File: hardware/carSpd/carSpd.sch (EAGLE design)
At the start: 0 parts

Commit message: Added power regulator schematics
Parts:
- added C1: 10uf, rcl:C-EUC0603K
- added C2: 22uf, rcl:C-EUC0603K
- added C3: 3.9nf, rcl:C-EUC0603K
- added C4, C7: .1uf, rcl:C-EUC0603K
- added C5: 10nf, rcl:C-EUC0603K
- added C6: .33uf, rcl:C-EUC0603K
- added IC1: DS3231/SO, adafruit:DS3231/SO
- added IC2: CP2102, silabs:CP2102
- added IC3: 7805DT, adafruit:7805DT
- added L1: CD54, inductor-sumida:CD54
- added L2: 10uh, rcl:L-USL3225M
- added R1: 10k, rcl:R-US_R0603
- added R2: 100k, rcl:R-US_R0603
- added R3: 6.8k, rcl:R-US_R0603
- added R4: 44.2k, rcl:R-US_R0603
- added S1, S2, S3, S4: SWITCH-MOMENTARY-2SMD-4, SparkFun-Electromechanical:SWITCH-MOMENTARY-2SMD-4
- added U$1: CH340G, ch340g:CH340G
- added U1: ATMEGA328P-AU, Atmel_By_element14_Batch_1-00:ATMEGA328P-AU
- added U2: MP2307, hybridair:MP2307
- added U3: ERC1602-4, hybridair:ERC1602-4
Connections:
- new net +12V: C1.1, C6.1, IC3.VI, R2.2, U2.IN
- new net +5V: C2.1, C7.1, IC3.VO, L1.1, L2.1, R4.1
- new net GND: C1.2, C2.2, C4.2, C6.2, C7.2, IC3.GND, R1.1, R3.1, U2.GND
- new net N$1: C5.2, U2.BS
- new net N$2: C5.1, L1.2, L2.2, U2.SW
- new net N$3: R1.2, R4.2, U2.FB
- new net N$5: C3.2, R3.2
- new net N$6: C3.1, U2.COMP
- new net N$7: C4.1, U2.SS
- new net N$9: R2.1, U2.EN
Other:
- note added: "12V comes from the car's accessory power rail, which is regulated down to 5V. The carSpd device itself shouldn't use more than 100ma."
- note added: "For option 1, use either the 10uh CD54 inductor or 10uh 3225 inductor. Either one should support at least 500ma of current saturation."
- note added: "ONLY USE ONE OPTION, DO NOT POPULATE BOTH AT ONCE"
- note added: "OPTION 1"
- note added: "OPTION 2"
- note added: "Option 1 is an untested DC-DC buck regulator, and Option 2 is a tested, backup linear regulator circuit. Option 1 is preferred due to its efficiency, but is untested so it may not work in production. Option 2 is simpler, less efficient, but should work as expected."
- note added: "POWER REGULATION"

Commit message: Added USB to serial schematics
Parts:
- removed IC3: 7805DT, adafruit:7805DT
- added C10, C11, C15, C9: 0.1uf, rcl:C-EUC0603K
- added C12: 10nf, rcl:C-EUC0603K
- added C13, C14: 18pf, rcl:C-EUC0603K
- added C8: 1uf, rcl:C-EUC0603K
- added JP1: USBSMD, SparkFun-Connectors:USBSMD
- added R6: 4.7k, rcl:R-US_R0603
- added R7: 10k, rcl:R-US_R0603
- added U4: ERC1602-4, hybridair:ERC1602-4
- added Y1: 12mhz, SparkFun-FreqCtrl:CRYSTALFIXED
- added Y2: (no value), SparkFun-FreqCtrl:CRYSTALSMD
- U3: value ERC1602-4 -> 7805DT; device hybridair:ERC1602-4 -> adafruit:7805DT
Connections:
- new net D+: IC2.D+, U$1.D+
- new net D-: IC2.D-, U$1.D-
- new net N$10: C11.1, IC2.DTR
- new net N$12: C10.1, IC2.VDD
- new net N$16: C15.1, U$1.DTR
- new net N$17: C12.1, U$1.V3
- new net N$18: C14.2, U$1.XO, Y1.2, Y2.2
- new net N$19: C13.2, U$1.XI, Y1.1, Y2.1
- new net N$4: IC2.!RST, R6.1
- new net N$8: IC2.!SUSPEND, R7.2
- new net RST: C11.2, C15.2
- new net RX: IC2.TXD, U$1.TX
- new net TX: IC2.RXD, U$1.RX
- net +12V: now also U3.VI; no longer IC3.VI
- net +5V: now also C8.1, C9.1, IC2.REGIN, IC2.VBUS, R6.2, U$1.VCC, U3.VO; no longer IC3.VO
- net GND: now also C10.2, C12.2, C13.1, C14.1, C8.2, C9.2, IC2.GND, IC2.GND@EXP, IC2.GND@M, R7.1, U$1.GND, U3.GND; no longer IC3.GND
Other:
- note added: "For option 1, use either an SMD axial crystal, or an SMD HC49 crystal. Change load capacitors as necessary."
- note added: "Option 1 is an untested CH340G serial circuit, and Option 2 is a tested, backup CP2102 serial circuit. Option 1 is preferred due to its price, but is untested so it may not work in production. Option 2 is more expensive, but will work just fine."
- note added: "The USB to serial circuit is used to allow the atmega328 to be programmed over USB, using the optiboot serial bootloader."
- note added: "USB to Serial"

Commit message: Added peripheral schematics
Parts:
- removed U4: ERC1602-4, hybridair:ERC1602-4
- added B1: BATTERY1220, Battery&Holder:BATTERY1220
- added C16, C20: 0.1uf, rcl:C-EUC0603K
- added C17, C19: 1uf, rcl:C-EUC0603K
- added C18: 10uf, rcl:C-EUC0603K
- added DISPLAY: ERC1602-4, hybridair:ERC1602-4
- added DISP_LED: (no value), SparkFun-Connectors:M021X02_NO_SILK
- added LED1, LED2, LED3, LED4: (no value), led:LEDCHIPLED_0805
- added Q1: 2n3904, SparkFun-DiscreteSemi:TRANSISTOR_NPNSOT23-3
- added R10, R9: 4.7k, rcl:R-US_R0603
- added R5: 10k, rcl:R-US_R0603
- added R8: 220, rcl:R-US_R0603
- added U$2: DS1820, Ava:DS1820
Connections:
- new net LED_PWM: R5.2
- new net N$11: Q1.B, R5.1
- new net N$13: DISP_LED.2, R8.1
- new net N$14: C17.2, DISPLAY.VOUT
- new net N$15: Q1.C, R8.2, R9.2
- new net N$20: C19.1, DISPLAY.CAP1P
- new net N$21: C19.2, DISPLAY.CAP1N
- new net N$23: LED1.A, LED2.A, LED3.A, LED4.A, R9.1
- new net N$27: B1.+, IC1.VBAT
- new net SCL: DISPLAY.SCL, IC1.SCL
- new net SDA: DISPLAY.SDA, IC1.SDA
- new net TEMP: R10.1, U$2.DQ
- net +5V: now also C16.1, C17.1, C18.1, C20.1, DISPLAY.PSB, DISPLAY.RS, DISPLAY.VDD, DISPLAY.XRESET, IC1.VCC, R10.2, U$2.VCC
- net GND: now also B1.-, C16.2, C18.2, C20.2, DISPLAY.CSB, DISPLAY.PSI2B, DISPLAY.VSS, DISP_LED.1, IC1.GND, IC1.NC, IC1.NC1, IC1.NC2, IC1.NC3, IC1.NC4, IC1.NC5, IC1.NC6, IC1.NC7, LED1.C, LED2.C, LED3.C, LED4.C, Q1.E, U$2.GND
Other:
- note added: "DISPLAY"
- note added: "Peripherals"
- note added: "RTC"
- note added: "TEMP"
- note added: "The DS3231 RTC is untested, but should wor according to the datasheet."

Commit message: Finished schematic, unverified
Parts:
- removed U1: ATMEGA328P-AU, Atmel_By_element14_Batch_1-00:ATMEGA328P-AU
- added C22, C23: 18pf, rcl:C-EUC0603K
- added C24, C25: 0.1uf, rcl:C-EUC0603K
- added D1, D2, D3: 5.1V, SparkFun-DiscreteSemi:DIODE-ZENER5.6V
- added JP2: AVR_ICSP, SparkFun-Connectors:AVR_SPI_PRG_6TESTPOINTS
- added JP3: USBSMD, SparkFun-Connectors:USBSMD
- added LED5: STATUS, led:LEDCHIPLED_0805
- added LED6: POWER, led:LEDCHIPLED_0805
- added R11: 10k, rcl:R-US_R0603
- added R12, R13: 4.7k, rcl:R-US_R0603
- added R14: 220, rcl:R-US_R0603
- added R15, R16, R17: 50k, rcl:R-US_R0603
- added R18: 1k, rcl:R-US_R0603
- added S5: RESET, SparkFun-Electromechanical:SWITCH-MOMENTARY-2SMD-1101NE
- added U$3, U$4, U$5: 5.1V, hybridair:ZMM5V1
- added U4: ATMEGA328P_TQFP, SparkFun-DigitalIC:ATMEGA328P_TQFP
- added Y3: 16mhz, SparkFun-FreqCtrl:CRYSTALSMD
- JP1: value USBSMD -> CAR_INPUT; device SparkFun-Connectors:USBSMD -> SparkFun-Connectors:M05PTH
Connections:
- new net INJ: JP1.3, R15.1
- new net LIGHTING: JP1.4, R17.1
- new net N$22: JP2.1, U4.PB4(MISO)
- new net N$24: C22.1, U4.PB6(XTAL1/TOSC1), Y3.2
- new net N$26: JP2.3, LED5.A, U4.PB5(SCK)
- new net N$28: S1.1, U4.PD6(AIN0)
- new net N$29: LED6.A, R18.1
- new net N$30: D2.C, R15.2, U$4.C, U4.PD2(INT0), U4.PD3(INT1)
- new net N$31: D1.C, R17.2, U$3.C, U4.PC0(ADC0)
- new net N$32: LED5.C, R14.1
- new net N$33: S3.1, U4.PB0(ICP)
- new net N$34: S2.1, U4.PD7(AIN1)
- new net N$35: S4.1, U4.PB1(OC1A)
- new net N$36: D3.C, R16.2, U$5.C, U4.PD5(T1)
- new net N$37: C23.1, U4.PB7(XTAL2/TOSC2), Y3.1
- new net VSS: JP1.2, R16.1
- net +12V: now also JP1.1
- net +5V: now also C24.1, C25.1, JP2.2, JP3.VBUS, R11.1, R12.1, R13.1, R18.2, U4.AVCC, U4.VCC@4, U4.VCC@6
- net D+: now also JP3.D+
- net D-: now also JP3.D-
- net GND: now also C22.2, C23.2, C24.2, C25.2, D1.A, D2.A, D3.A, JP1.5, JP2.6, JP3.GND, LED6.C, R14.2, S1.2, S2.2, S3.2, S4.2, S5.1, U$3.A, U$4.A, U$5.A, U4.AGND, U4.GND@3, U4.GND@5
- net LED_PWM: now also JP2.4, U4.PB3(MOSI/OC2)
- net RST: now also JP2.5, R11.2, S5.2, U4.PC6(/RESET)
- net RX: now also U4.PD0(RXD)
- net SCL: now also R13.2, U4.PC5(ADC5/SCL)
- net SDA: now also R12.2, U4.PC4(ADC4/SDA)
- net TX: now also U4.PD1(TXD)
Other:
- note added: "The DS3231 RTC is untested, but should work according to the datasheet."
- note added: "Two crystal footprints are provided for part compatibility, use only one."
- note added: "Two diode footprints are provided for part compatibility, use only one."
- note removed: "For option 1, use either an SMD axial crystal, or an SMD HC49 crystal. Change load capacitors as necessary."
- note removed: "The DS3231 RTC is untested, but should wor according to the datasheet."

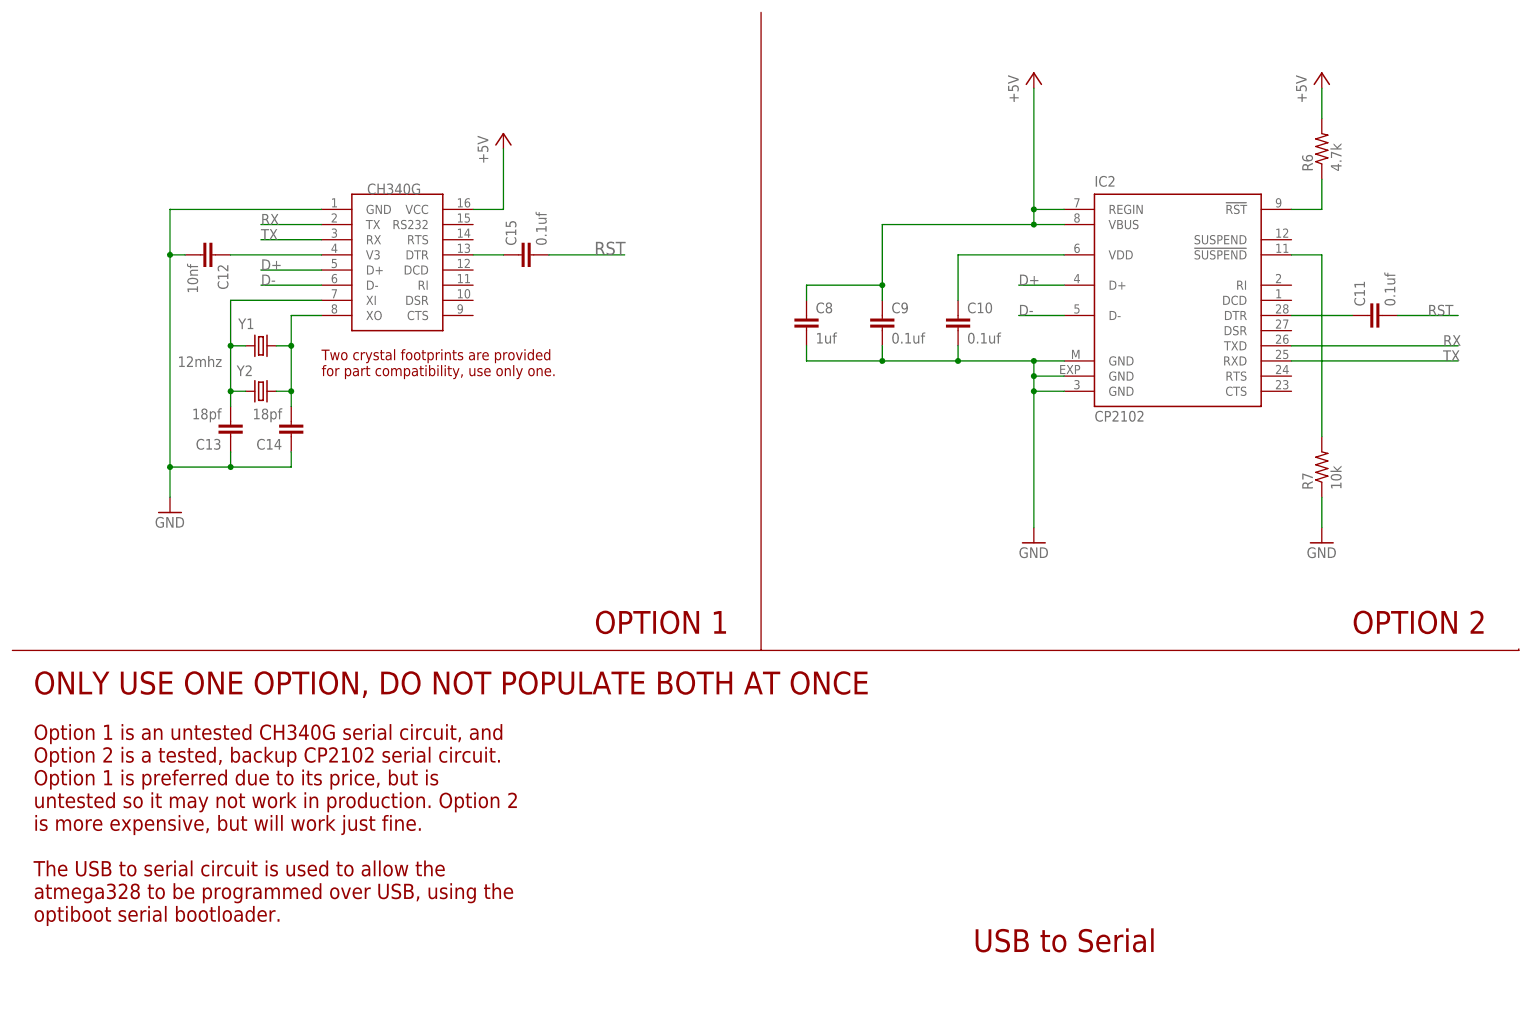
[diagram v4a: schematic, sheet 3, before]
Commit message: Removed the CH340G, supporting parts made it cost as much as a CP2102
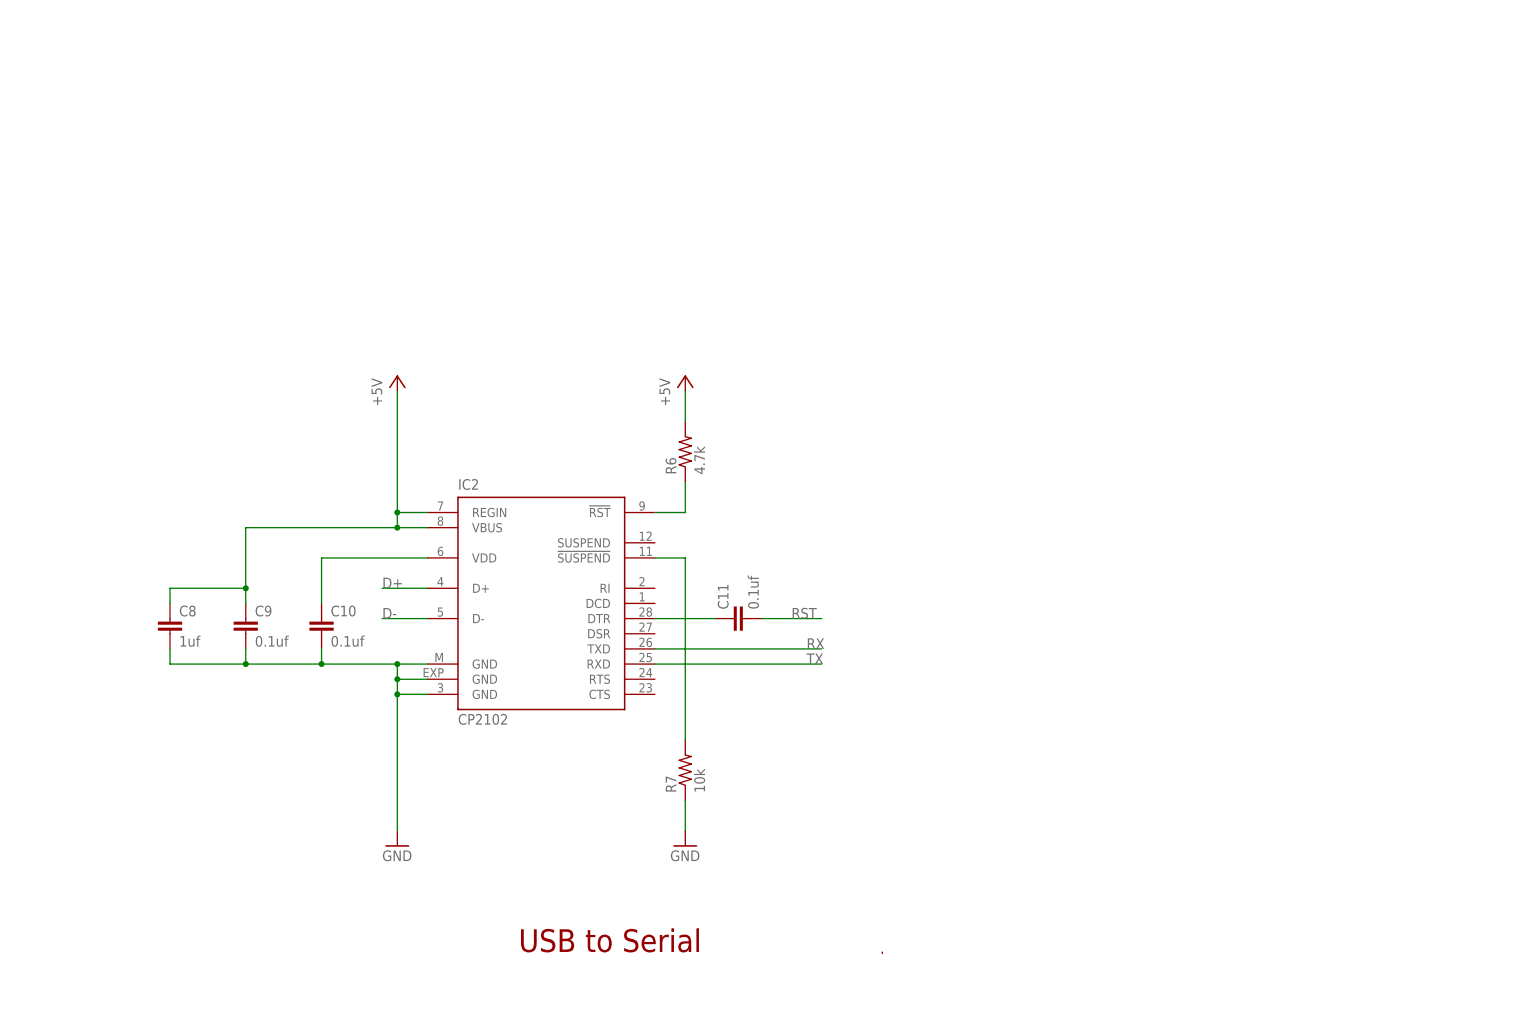
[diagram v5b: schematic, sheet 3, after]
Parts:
- removed C12: 10nf, rcl:C-EUC0603K
- removed C13, C14: 18pf, rcl:C-EUC0603K
- removed C15: 0.1uf, rcl:C-EUC0603K
- removed JP1: CAR_INPUT, SparkFun-Connectors:M05PTH
- removed U$1: CH340G, ch340g:CH340G
- removed Y1: 12mhz, SparkFun-FreqCtrl:CRYSTALFIXED
- removed Y2: (no value), SparkFun-FreqCtrl:CRYSTALSMD
- added STANDOFF1, STANDOFF2, STANDOFF3, STANDOFF4: STAND-OFF, SparkFun-Electromechanical:STAND-OFF
- added SV1: CAR_INPUT, con-lsta:FE05W
- S1, S2, S3, S4: value SWITCH-MOMENTARY-2SMD-4 -> SWITCH-MOMENTARY-2SMD-1101NE; device SparkFun-Electromechanical:SWITCH-MOMENTARY-2SMD-4 -> SparkFun-Electromechanical:SWITCH-MOMENTARY-2SMD-1101NE
- Y3: device SparkFun-FreqCtrl:CRYSTALSMD -> SparkFun-FreqCtrl:CRYSTAL5X3
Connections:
- removed net N$16: C15.1, U$1.DTR
- removed net N$17: C12.1, U$1.V3
- removed net N$18: C14.2, U$1.XO, Y1.2, Y2.2
- removed net N$19: C13.2, U$1.XI, Y1.1, Y2.1
- net +12V: now also SV1.1; no longer JP1.1
- net +5V: no longer U$1.VCC
- net D+: no longer U$1.D+
- net D-: no longer U$1.D-
- net GND: now also SV1.5; no longer C12.2, C13.1, C14.1, JP1.5, U$1.GND
- net INJ: now also SV1.3; no longer JP1.3
- net LIGHTING: now also SV1.4; no longer JP1.4
- net RST: no longer C15.2
- net RX: no longer U$1.TX
- net TX: no longer U$1.RX
- net VSS: now also SV1.2; no longer JP1.2
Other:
- note added: "Two inductor footprints are provided for part compatibility, use only one."
- note removed: "For option 1, use either the 10uh CD54 inductor or 10uh 3225 inductor. Either one should support at least 500ma of current saturation."
- note removed: "Option 1 is an untested CH340G serial circuit, and Option 2 is a tested, backup CP2102 serial circuit. Option 1 is preferred due to its price, but is untested so it may not work in production. Option 2 is more expensive, but will work just fine."
- note removed: "The USB to serial circuit is used to allow the atmega328 to be programmed over USB, using the optiboot serial bootloader."
- note removed: "Two crystal footprints are provided for part compatibility, use only one."
- moved on the sheet: C10, C11, C8, C9, IC2, R6, R7

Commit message: Schematic cleanup
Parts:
- removed DISP_LED: (no value), SparkFun-Connectors:M021X02_NO_SILK
- removed STANDOFF1, STANDOFF2, STANDOFF3, STANDOFF4: STAND-OFF, SparkFun-Electromechanical:STAND-OFF
- removed U$3, U$4, U$5: 5.1V, hybridair:ZMM5V1
- removed Y3: 16mhz, SparkFun-FreqCtrl:CRYSTAL5X3
- added D4, D5, D6: 5.1V, hybridair:ZMM5V1
- added Y1: 16MHZ, SparkFun-FreqCtrl:RESONATOR16MHZ
- added Y2: 16mhz, SparkFun-FreqCtrl:CRYSTAL5X3
- B1: value BATTERY1220 -> CR1220
- C17, C19, C5, C8: device rcl:C-EUC0603K -> rcl:C-EUC0805K
- C4, C7: value .1uf -> 0.1uf
- DISPLAY: value ERC1602-4 -> ERC1602-4SMD-LED; device hybridair:ERC1602-4 -> hybridair:ERC1602-4SMD-LED
- R10, R12, R13, R2, R6, R9: device rcl:R-US_R0603 -> rcl:R-US_R0805
- R14: value 220 -> 270
- R15, R16, R17: value 50k -> 47k; device rcl:R-US_R0603 -> rcl:R-US_R0805
- R18: value 1k -> 2.7k
- R8: value 220 -> 150
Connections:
- removed net N$13: DISP_LED.2, R8.1
- new net N$16: DISPLAY.LED+, R8.1
- net GND: now also C23.1, D4.A, D5.A, D6.A, DISPLAY.LED-, Y1.2; no longer C23.2, DISP_LED.1, U$3.A, U$4.A, U$5.A
- net N$24: now also Y1.1, Y2.2; no longer Y3.2
- net N$30: now also D5.C; no longer U$4.C
- net N$31: now also D4.C; no longer U$3.C
- net N$36: now also D6.C; no longer U$5.C
- net N$37: now also C23.2, Y1.3, Y2.1; no longer C23.1, Y3.1
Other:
- note added: "Two crystal/ resonator footprints are provided for part compatibility, use only one."
- moved on the sheet: C17, C19, C22, C23, C24, C25, D1, D2, D3, JP2, LED5, R11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

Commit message: Modified and added parts list
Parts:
- C6: value .33uf -> 100uf; device rcl:C-EUC0603K -> ELL-i-Passives:CPOLD
- C7: value 0.1uf -> 10uf
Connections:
- net +12V: now also C6.+; no longer C6.1
- net GND: now also C6.-; no longer C6.2
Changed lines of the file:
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@@
 <layer number="56" name="wert" color="7" fill="1" visible="yes" active="no"/>
 <layer number="57" name="tCAD" color="7" fill="1" visible="yes" active="no"/>
+<layer number="58" name="bCopper" color="7" fill="1" visible="no" active="no"/>
 <layer number="59" name="tCarbon" color="7" fill="1" visible="yes" active="no"/>
 <layer number="60" name="bCarbon" color="7" fill="1" visible="yes" active="no"/>
@@
 <layer number="250" name="Descript" color="7" fill="1" visible="no" active="no"/>
 <layer number="251" name="SMDround" color="7" fill="1" visible="no" active="no"/>
+<layer number="253" name="Extra" color="7" fill="1" visible="yes" active="yes"/>
 <layer number="254" name="cooling" color="7" fill="1" visible="no" active="yes"/>
 <layer number="255" name="HELP" color="7" fill="1" visible="yes" active="yes"/>
@@
 <part name="P+3" library="supply1" deviceset="+12V" device=""/>
 <part name="U3" library="adafruit" deviceset="78*" device="DT" technology="05"/>
-<part name="C6" library="rcl" deviceset="C-EU" device="C0603K" value=".33uf"/>
-<part name="C7" library="rcl" deviceset="C-EU" device="C0603K" value="0.1uf"/>
+<part name="C7" library="rcl" deviceset="C-EU" device="C0603K" value="10uf"/>
 <part name="P+4" library="supply1" deviceset="+12V" device=""/>
 <part name="P+5" library="supply1" deviceset="+5V" device=""/>
@@
 <part name="FRAME5" library="frames" deviceset="A5L-LOC" device=""/>
 <part name="Y1" library="SparkFun-FreqCtrl" deviceset="RESONATOR" device="16MHZ" value="16MHZ"/>
+<part name="C6" library="ELL-i-Passives" deviceset="CPOL" device="D" value="100uf"/>
 </parts>
 <sheets>
@@
 <instances>
 <instance part="U3" gate="A1" x="208.28" y="129.54"/>
-<instance part="C6" gate="G$1" x="190.5" y="121.92"/>
 <instance part="C7" gate="G$1" x="226.06" y="121.92"/>
 <instance part="P+4" gate="1" x="190.5" y="142.24"/>
@@
 <instance part="P+3" gate="1" x="96.52" y="167.64"/>
 <instance part="FRAME4" gate="G$1" x="0" y="0"/>
+<instance part="C6" gate="G$1" x="190.5" y="121.92"/>
 </instances>
 <busses>
@@
 <net name="+12V" class="0">
 <segment>
-<pinref part="C6" gate="G$1" pin="1"/>
 <pinref part="P+4" gate="1" pin="+12V"/>
 <wire x1="190.5" y1="124.46" x2="190.5" y2="129.54" width="0.1524" layer="91"/>
@@
 <wire x1="190.5" y1="129.54" x2="198.12" y2="129.54" width="0.1524" layer="91"/>
 <junction x="190.5" y="129.54"/>
+<pinref part="C6" gate="G$1" pin="+"/>
 </segment>
 <segment>
@@
 <net name="GND" class="0">
 <segment>
-<pinref part="C6" gate="G$1" pin="2"/>
 <wire x1="190.5" y1="116.84" x2="190.5" y2="114.3" width="0.1524" layer="91"/>
 <pinref part="GND2" gate="1" pin="GND"/>
@@
 <wire x1="208.28" y1="114.3" x2="226.06" y2="114.3" width="0.1524" layer="91"/>
 <wire x1="226.06" y1="114.3" x2="226.06" y2="116.84" width="0.1524" layer="91"/>
-</segment>
-<segment>
+<pinref part="C6" gate="G$1" pin="-"/>
+</segment>
+<segment>
